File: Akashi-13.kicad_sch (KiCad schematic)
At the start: 5 parts, among them J1 Conn_02x35_Odd_Even, J2 Conn_02x35_Odd_Even, J3 N7E50-Q516RB-50, J4 J0011D01BNL, U1 LAN9220-ABZJ

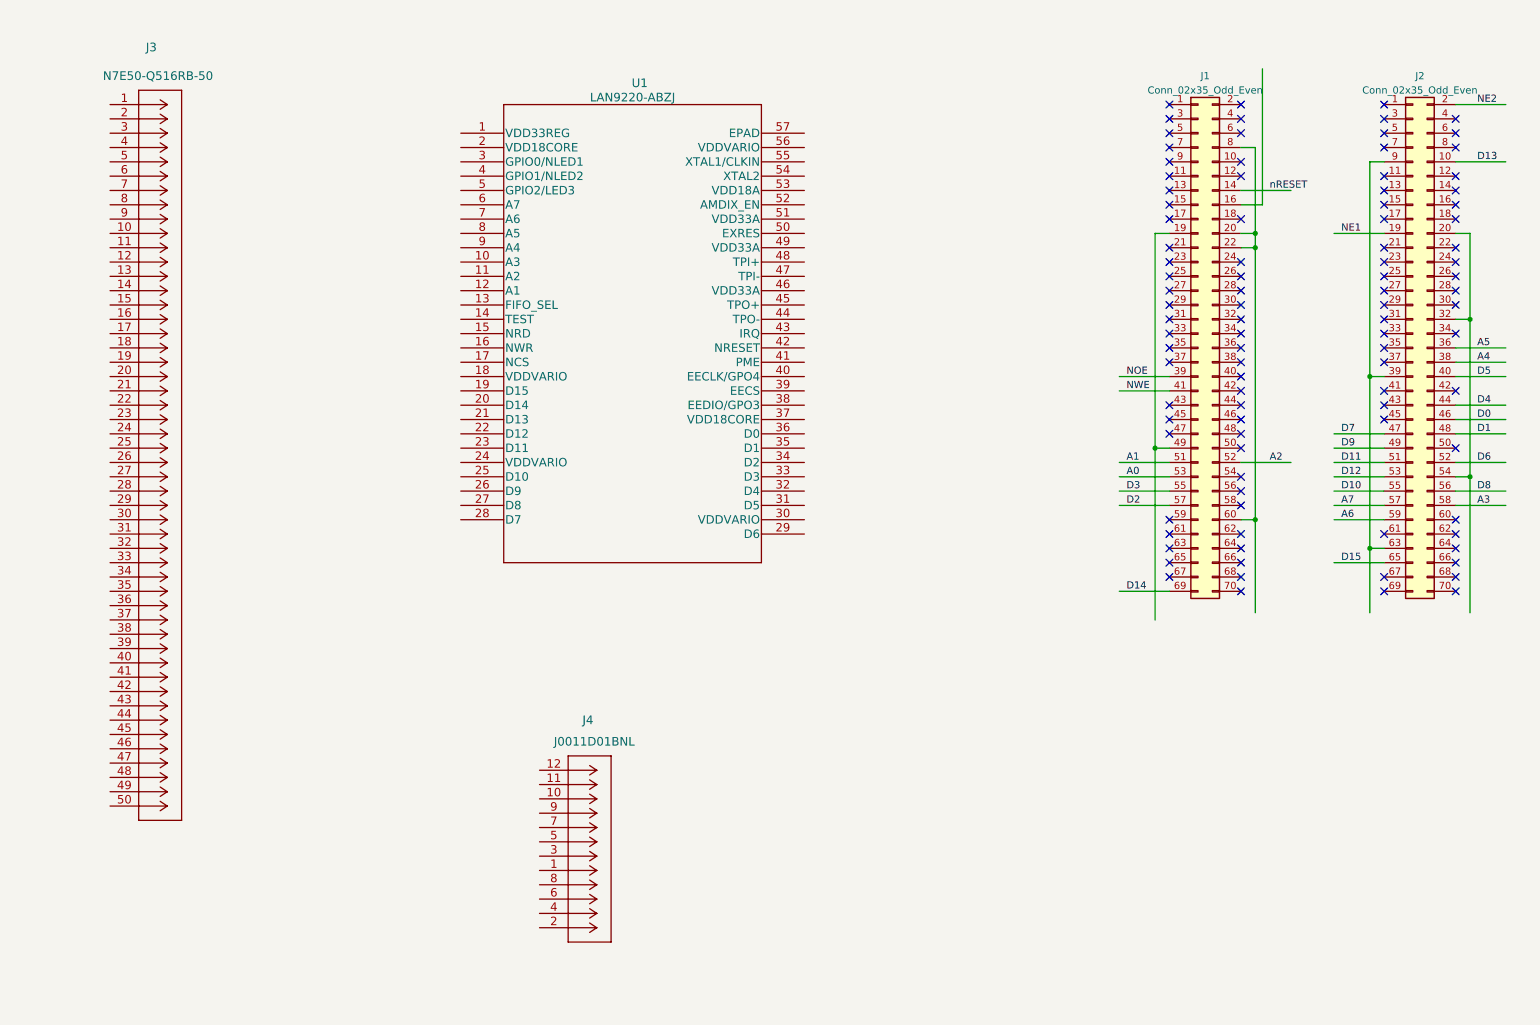
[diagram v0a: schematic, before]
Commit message: Drawing schematics.
Done round the RF-45 connectors.

Connecting the power of the LAN9220.
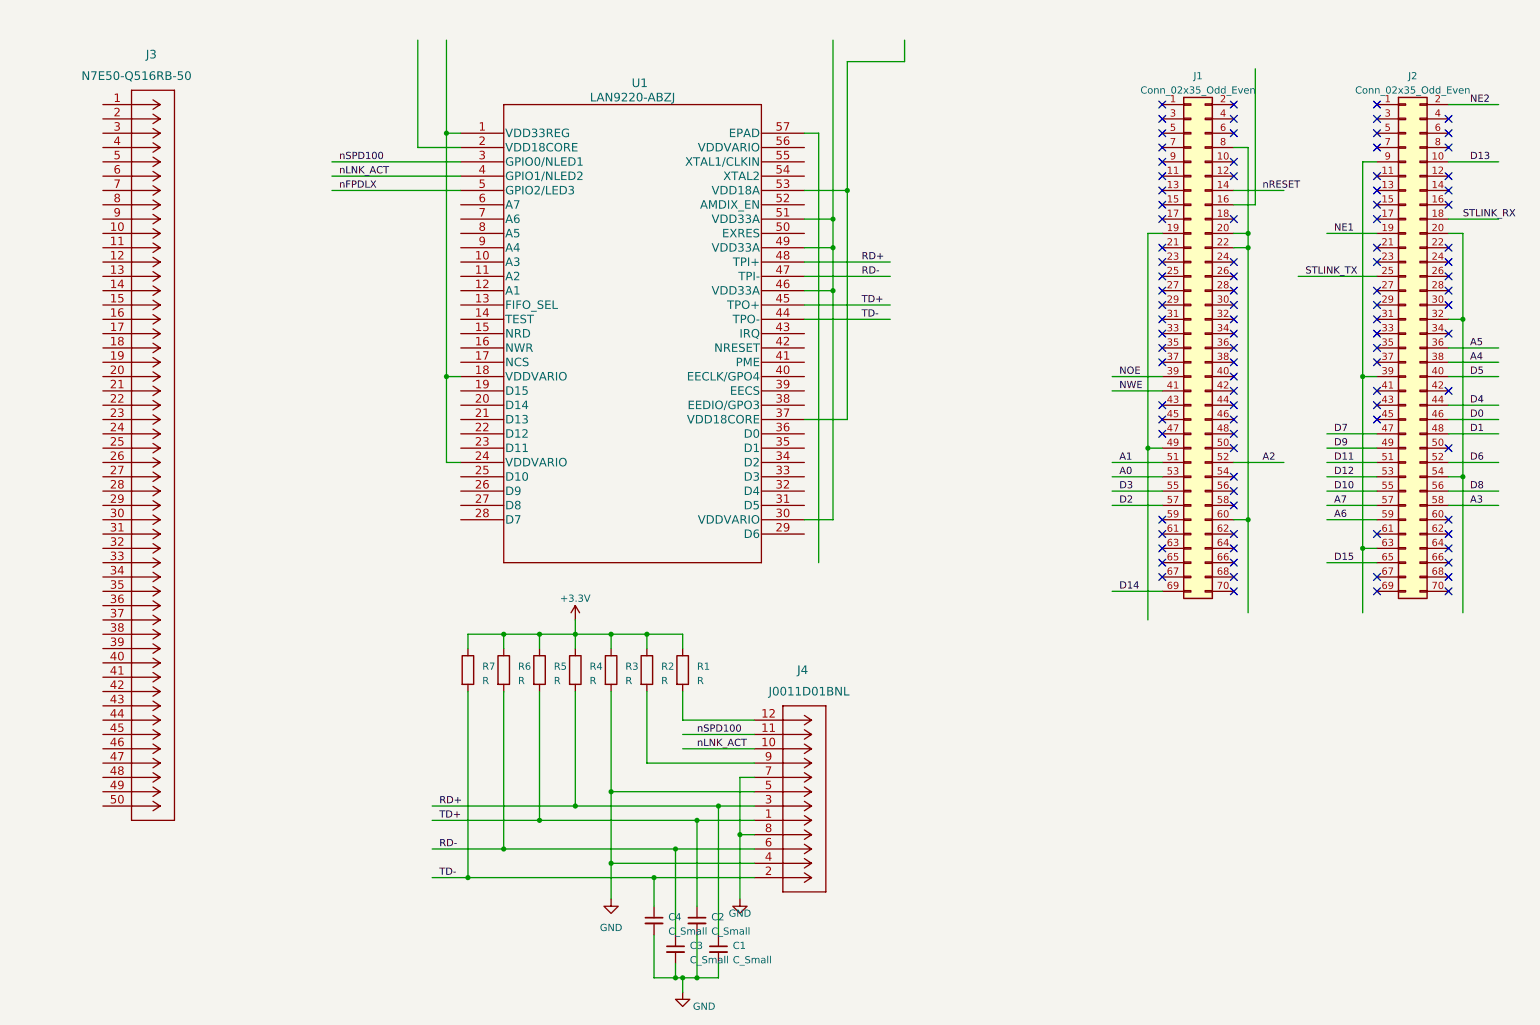
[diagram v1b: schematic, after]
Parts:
- added C1, C2, C3, C4: C_Small, symbol Device:C_Small
- added R1, R2, R3, R4, R5, R6, R7: R, symbol Device:R
- U1: footprint MyFootprint:LAN9220-ABZJ -> Package_DFN_QFN:QFN-56-1EP_8x8mm_P0.5mm_EP5.9x5.9mm
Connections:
- net at U1.1 (VDD33REG): now also U1.18 (VDDVARIO), U1.24 (VDDVARIO)
- net nSPD100: now reaches U1.3 (GPIO0/NLED1)
- net nSPD100: now also J4.11
- net at U1.30 (VDDVARIO): now also U1.46 (VDD33A), U1.49 (VDD33A), U1.51 (VDD33A)
- net at U1.37 (VDD18CORE): now also U1.53 (VDD18A)
- net nLNK_ACT: now reaches U1.4 (GPIO1/NLED2)
- net nLNK_ACT: now also J4.10
- net TD-: now reaches U1.44 (TPO-)
- net TD-: now also J4.2, C4.1, R7.2
- net TD+: now reaches U1.45 (TPO+)
- net TD+: now also J4.1, C2.1, R5.2
- net RD-: now reaches U1.47 (TPI-)
- net RD-: now also J4.6, C3.1, R6.2
- net RD+: now reaches U1.48 (TPI+)
- net RD+: now also J4.3, C1.1, R4.2
- net nFPDLX: now reaches U1.5 (GPIO2/LED3)
- net at J4.12: now also R1.2
- net GND: now reaches J4.4
- net GND: now also J4.5, J4.7, J4.8, C1.2, C2.2, C3.2, C4.2, R3.2
- net at J4.9: now also R2.2
- net STLINK_RX: now reaches J2.18 (Pin_18)
- net STLINK_TX: now reaches J2.25 (Pin_25)
- new net +3.3V: R1.1, R2.1, R3.1, R4.1, R5.1, R6.1, R7.1
- no-connect marks 98 -> 96
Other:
- moved on the sheet: J1, J2, J4

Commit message: Added EEPROM
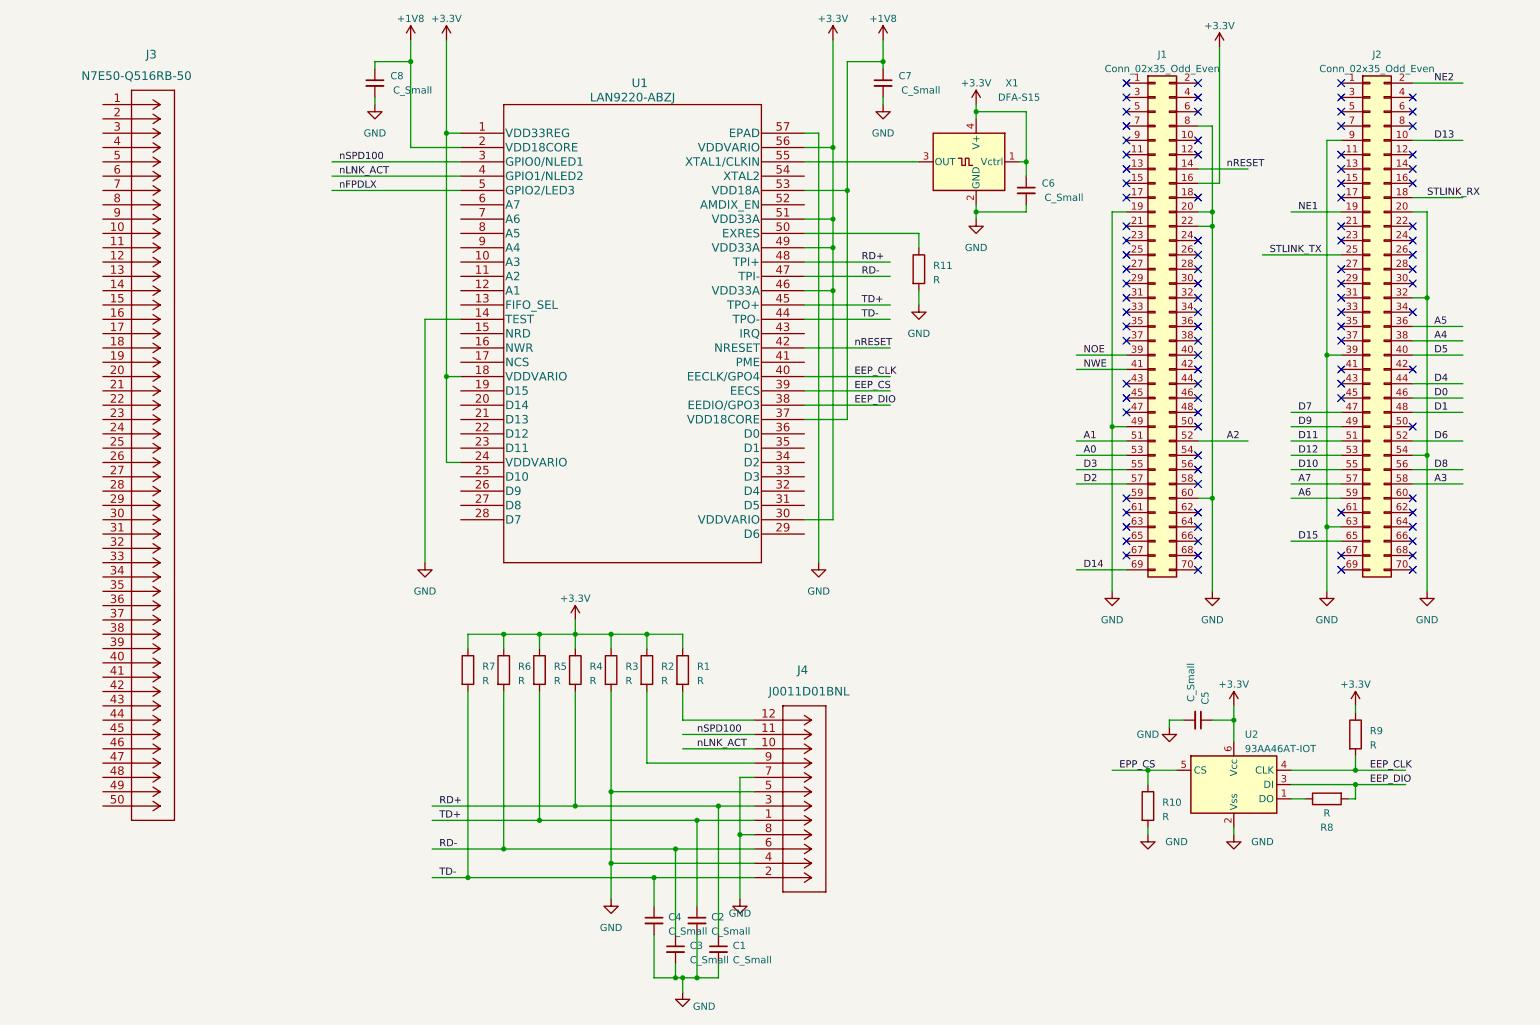
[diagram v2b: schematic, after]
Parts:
- added C5, C6, C7, C8: C_Small, symbol Device:C_Small
- added R10, R11, R8, R9: R, symbol Device:R
- added U2: 93AA46AT-IOT, Package_TO_SOT_SMD:SOT-23-6, symbol Memory_EEPROM:93AAxxAT-xOT
- added X1: DFA-S15, Oscillator:Oscillator_SMD_Fordahl_DFAS15-4Pin_5.0x3.2mm, symbol Oscillator:DFA-S15
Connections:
- net +3.3V: now also J1.16 (Pin_16), U1.1 (VDD33REG), U1.18 (VDDVARIO), U1.24 (VDDVARIO), U1.30 (VDDVARIO), U1.46 (VDD33A), U1.49 (VDD33A), U1.51 (VDD33A), U1.56 (VDDVARIO), C5.1, C6.1, R9.1, U2.6 (Vcc), X1.1 (Vctrl), X1.4 (V+)
- net GND: now also J1.19 (Pin_19), J1.20 (Pin_20), J1.22 (Pin_22), J1.49 (Pin_49), J1.60 (Pin_60), J1.8 (Pin_8), J2.20 (Pin_20), J2.32 (Pin_32), J2.39 (Pin_39), J2.54 (Pin_54), J2.63 (Pin_63), J2.9 (Pin_9), U1.14 (TEST), U1.57 (EPAD), C5.2, C6.2, C7.2, C8.2, R10.2, R11.2, U2.2 (Vss), X1.2 (GND)
- net nRESET: now also U1.42 (NRESET)
- net +1V8: now reaches U1.2 (VDD18CORE)
- net +1V8: now also U1.37 (VDD18CORE), U1.53 (VDD18A), C7.1, C8.1
- net EEP_DIO: now reaches U1.38 (EEDIO/GPO3)
- net EEP_DIO: now also R8.2, U2.3 (DI)
- net EEP_CS: now reaches U1.39 (EECS)
- net EEP_CLK: now reaches U1.40 (EECLK/GPO4)
- net EEP_CLK: now also R9.2, U2.4 (CLK)
- net at U1.50 (EXRES): now also R11.1
- net at U1.55 (XTAL1/CLKIN): now also X1.3 (OUT)
- new net: R8.1, U2.1 (DO)
- new net EPP_CS: R10.1, U2.5 (CS)
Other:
- moved on the sheet: J1, J2

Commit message: ST Link VCOM changed. IRQ/WAKE UP changed.
ST LINK vcom are moved from USART3 to LPUART1
Now, we don't need extra wireling.
Alternatively, short bridged of the baord have to be modified.

IQR/WAKEUP pins are moved. Now. we can cut two extra pins of
morpho connectors to reduce the pin force.
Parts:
- removed J3: N7E50-Q516RB-50, MyFootprint:N7E50-Q516RB-50, symbol CF_Socket:N7E50-Q516RB-50
- added D1: LED, LED_THT:LED_D3.0mm, symbol Device:LED
- added JP1: SolderJumper_2_Open, Jumper:SolderJumper-2_P1.3mm_Open_TrianglePad1.0x1.5mm, symbol Jumper:SolderJumper_2_Open
- added R12: R, Resistor_SMD:R_0603_1608Metric_Pad0.98x0.95mm_HandSolder, symbol Device:R
- C1, C2, C3, C4, C5, C6, C7, C8: footprint (none) -> Capacitor_SMD:C_0603_1608Metric_Pad1.08x0.95mm_HandSolder
- R1, R10, R11, R2, R3, R4, R5, R6, R7, R8, R9: footprint (none) -> Resistor_SMD:R_0603_1608Metric_Pad0.98x0.95mm_HandSolder
- renumbered J4 to J3
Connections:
- net NE1 is gone; now on net nE1: J2.19 (Pin_19)
- net NOE is gone; now on net nOE: J1.39 (Pin_39)
- net NWE is gone; now on net nWE: J1.41 (Pin_41)
- net +3.3V: now also R12.1
- net A1: now also U1.12 (A1)
- net A2: now also U1.11 (A2)
- net A3: now also U1.10 (A3)
- net A4: now also U1.9 (A4)
- net A5: now also U1.8 (A5)
- net A6: now also U1.7 (A6)
- net A7: now also U1.6 (A7)
- net D0: now also U1.36 (D0)
- net D1: now also U1.35 (D1)
- net D10: now also U1.25 (D10)
- net D11: now also U1.23 (D11)
- net D12: now also U1.22 (D12)
- net D13: now also U1.21 (D13)
- net D14: now also U1.20 (D14)
- net D15: now also U1.19 (D15)
- net D2: now also U1.34 (D2)
- net D3: now also U1.33 (D3)
- net D4: now also U1.32 (D4)
- net D5: now also U1.31 (D5)
- net D6: now also U1.29 (D6)
- net D7: now also U1.28 (D7)
- net D8: now also U1.27 (D8)
- net D9: now also U1.26 (D9)
- net GND: now also U1.13 (FIFO_SEL), JP1.2 (B)
- net nFPDLX: now also D1.1 (K)
- net nOE: now reaches U1.15 (NRD)
- net nWE: now reaches U1.16 (NWR)
- net nE1: now reaches U1.17 (NCS)
- net WAKEUP: now reaches U1.41 (PME)
- net WAKEUP: now also J1.28 (Pin_28)
- net IRQ: now reaches U1.43 (IRQ)
- net IRQ: now also J1.32 (Pin_32)
- net AMDIX_EN: now reaches U1.52 (AMDIX_EN)
- net AMDIX_EN: now also JP1.1 (A)
- net NE2: no longer names the net of J2.2 (Pin_2)
- net STLINK_RX: no longer names the net of J2.18 (Pin_18)
- net STLINK_TX: no longer names the net of J2.25 (Pin_25)
- new net: D1.2 (A), R12.2
- no-connect marks 96 -> 98
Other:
- note added: "The WAKEUP and IRQ signal have to be pulled up by MCU."
- moved on the sheet: C1, C2, C3, C4, C6, C7, C8, J3, R1, R11, R2, R3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

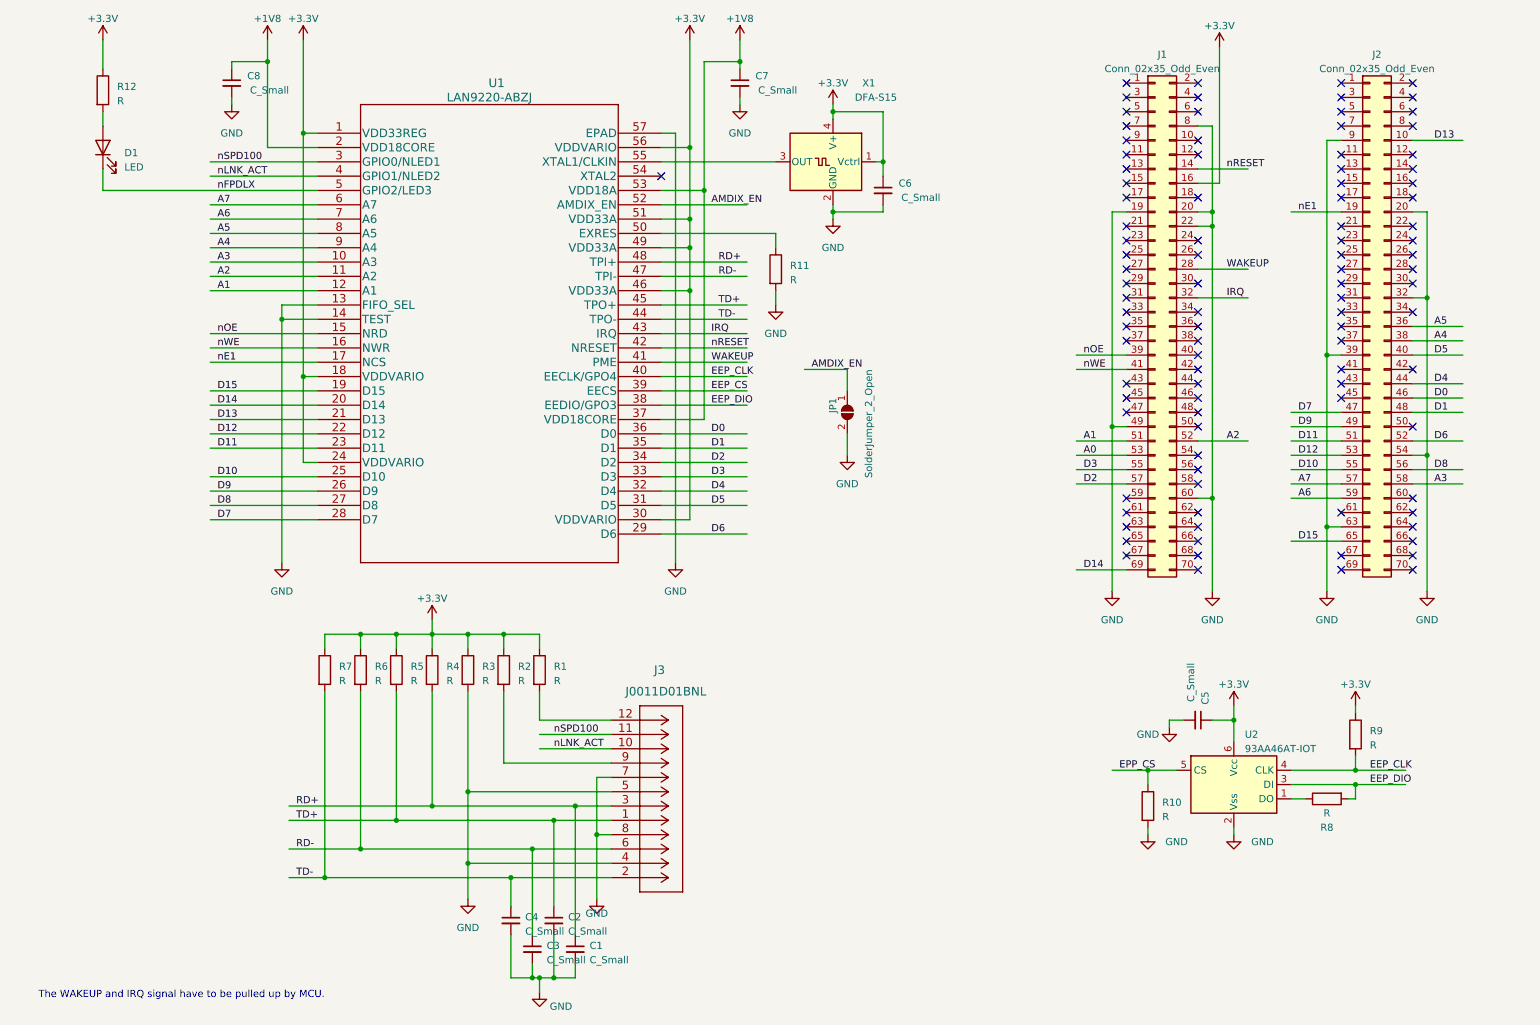
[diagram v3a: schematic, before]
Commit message: Finished to input schematics.
ERC OK.
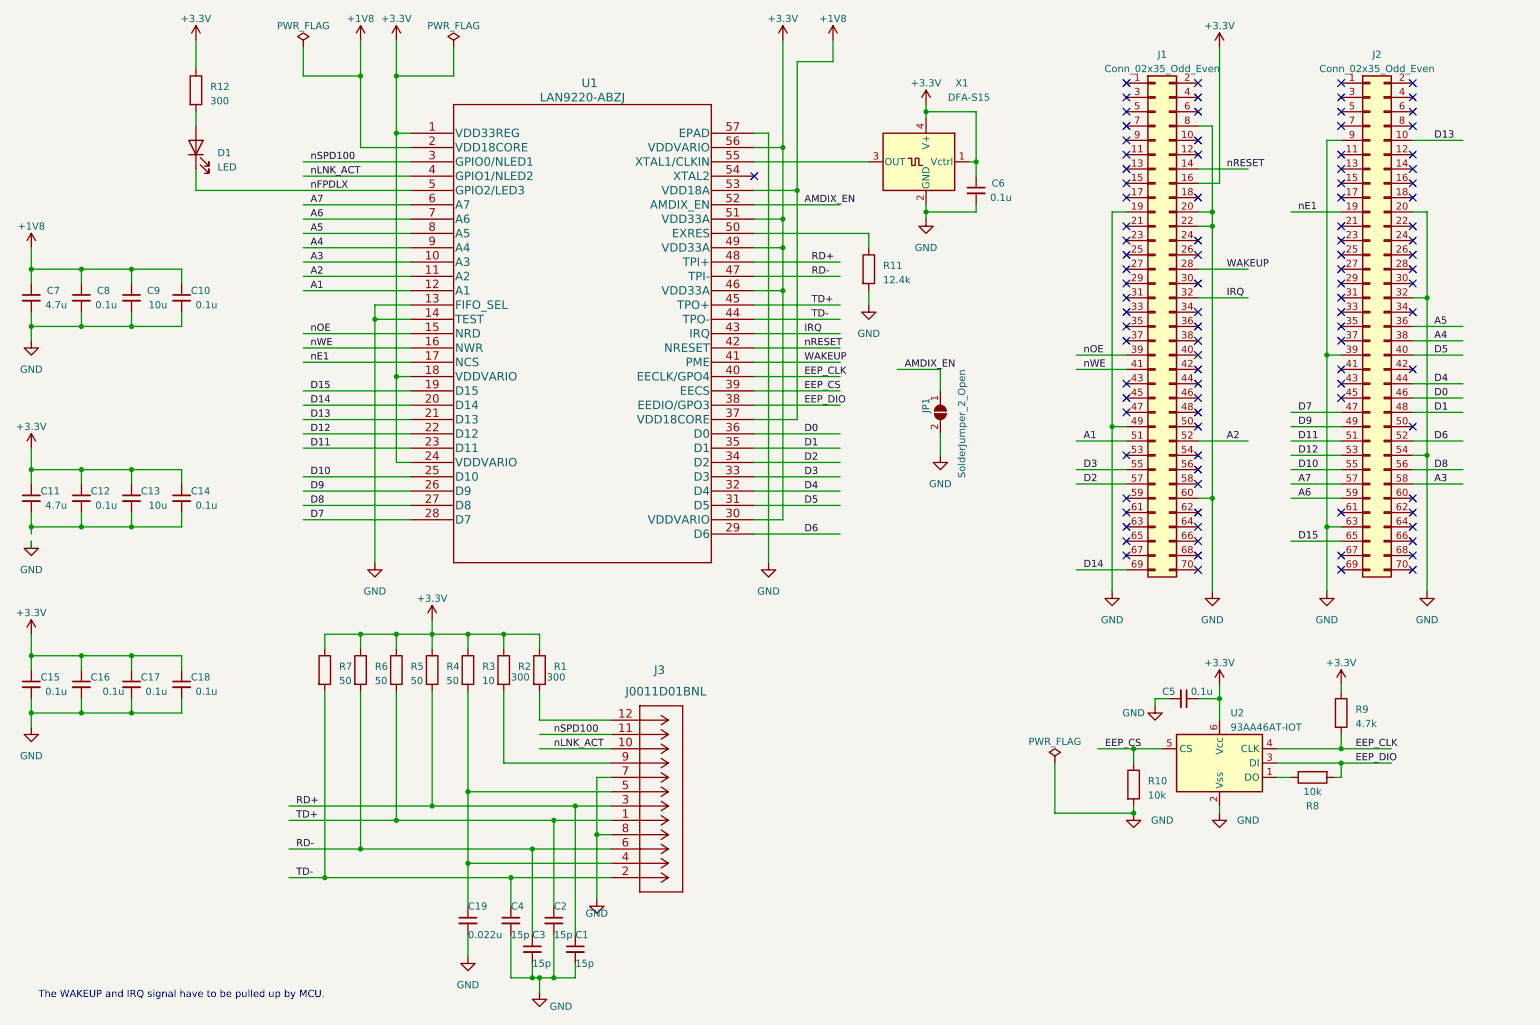
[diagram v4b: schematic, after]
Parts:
- added C10, C12, C14, C15, C16, C17, C18: 0.1u, Capacitor_SMD:C_0603_1608Metric_Pad1.08x0.95mm_HandSolder, symbol Device:C_Small
- added C11: 4.7u, Capacitor_SMD:C_0603_1608Metric_Pad1.08x0.95mm_HandSolder, symbol Device:C_Small
- added C13, C9: 10u, Capacitor_SMD:C_0603_1608Metric_Pad1.08x0.95mm_HandSolder, symbol Device:C_Small
- added C19: 0.022u, Capacitor_SMD:C_0603_1608Metric_Pad1.08x0.95mm_HandSolder, symbol Device:C_Small
- C1, C2, C3, C4: value C_Small -> 15p
- C5, C6, C8: value C_Small -> 0.1u
- C7: value C_Small -> 4.7u
- R1, R12, R2: value R -> 300
- R10, R8: value R -> 10k
- R11: value R -> 12.4k
- R3: value R -> 10
- R4, R5, R6, R7: value R -> 50
- R9: value R -> 4.7k
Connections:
- net EPP_CS is gone; now on net EEP_CS: R10.1, U2.5 (CS)
- net +1V8: now also C10.1, C9.1
- net +3.3V: now also C11.1, C12.1, C13.1, C14.1, C15.1, C16.1, C17.1, C18.1
- net GND: now also C10.2, C15.2, C16.2, C17.2, C18.2, C19.2, C9.2; no longer J3.4, J3.5, R3.2
- net A0: no longer names the net of J1.53 (Pin_53)
- new net: C11.2, C12.2, C13.2, C14.2
- new net: C19.1, J3.4, J3.5, R3.2
- no-connect marks 98 -> 99
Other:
- moved on the sheet: C5, C6, D1, JP1, R10, R11, R12, R8, R9, U1, U2, X1
